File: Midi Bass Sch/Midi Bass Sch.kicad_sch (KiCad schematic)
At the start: 0 parts

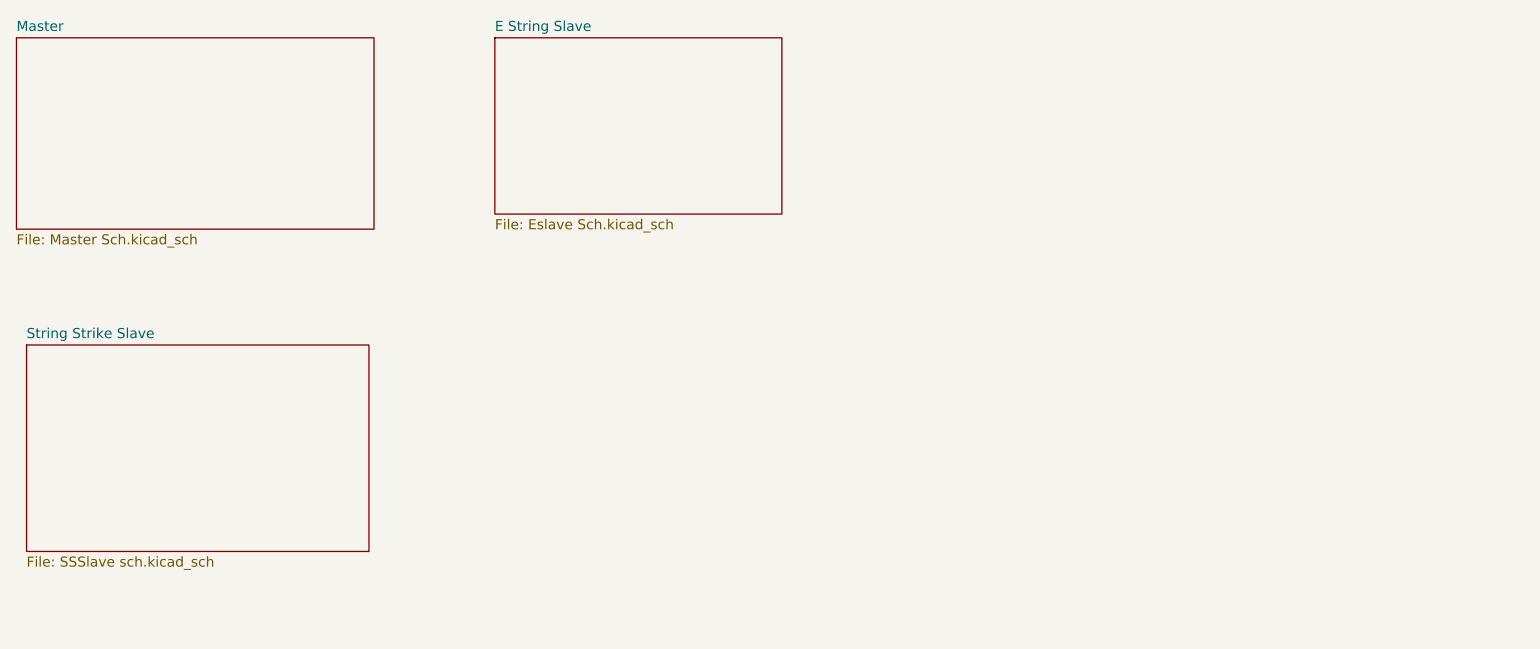
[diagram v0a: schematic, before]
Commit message: updated schematic to include all slaves
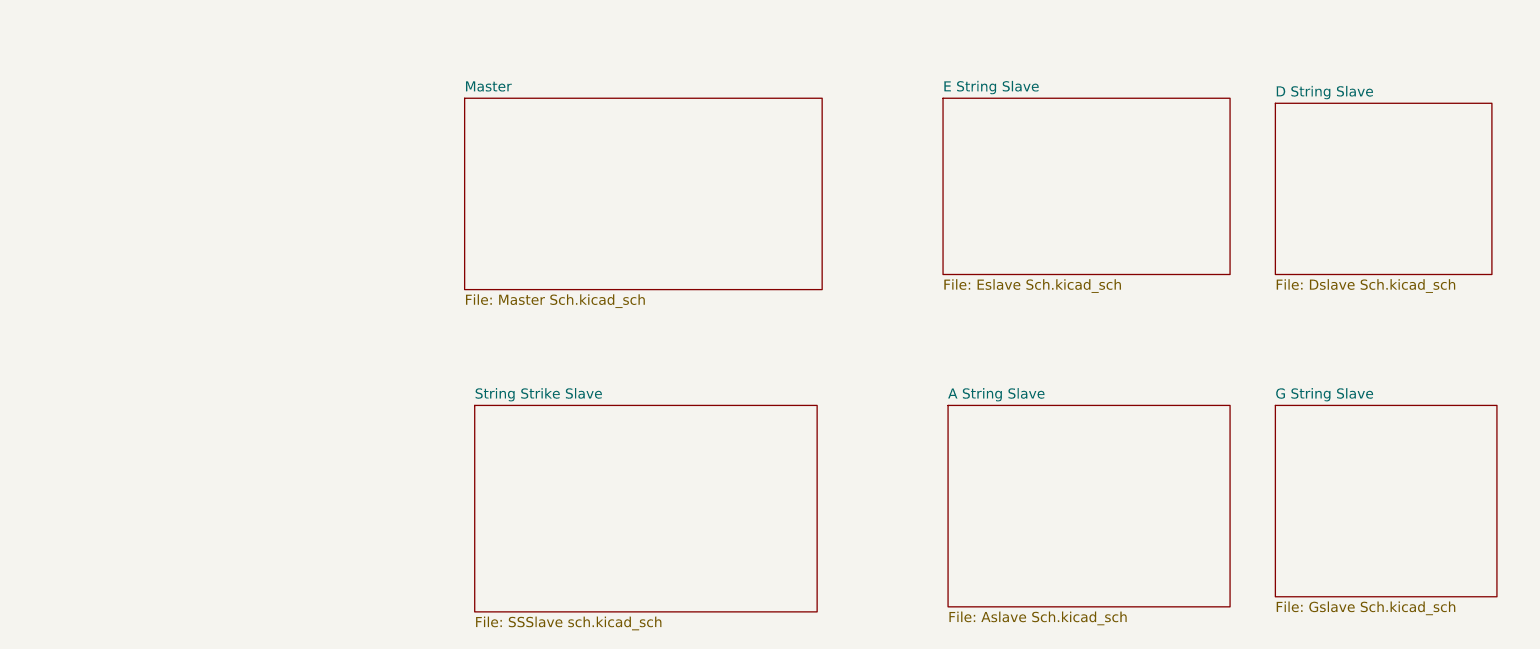
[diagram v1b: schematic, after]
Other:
- added sheet A String Slave (Aslave Sch.kicad_sch)
- added sheet D String Slave (Dslave Sch.kicad_sch)
- added sheet G String Slave (Gslave Sch.kicad_sch)
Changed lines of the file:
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@@
 	(paper "A4")
 	(sheet
-		(at 40.64 43.815)
+		(at 97.155 51.435)
 		(size 45.085 24.13)
 		(fields_autoplaced yes)
@@
 		)
 		(property "Sheetname" "Master"
-			(at 40.64 43.1034 0)
+			(at 97.155 50.7234 0)
 			(effects
 				(font
@@
 		)
 		(property "Sheetfile" "Master Sch.kicad_sch"
-			(at 40.64 68.5296 0)
+			(at 97.155 76.1496 0)
 			(effects
 				(font
@@
 	)
 	(sheet
-		(at 100.965 43.815)
+		(at 199.39 52.07)
+		(size 27.305 21.59)
+		(fields_autoplaced yes)
+		(stroke
+			(width 0.1524)
+			(type solid)
+		)
+		(fill
+			(color 255 255 194 1.0000)
+		)
+		(property "Sheetname" "D String Slave"
+			(at 199.39 51.3584 0)
+			(effects
+				(font
+					(size 1.27 1.27)
+				)
+				(justify left bottom)
+			)
+		)
+		(property "Sheetfile" "Dslave Sch.kicad_sch"
+			(at 199.39 74.2446 0)
+			(effects
+				(font
+					(size 1.27 1.27)
+				)
+				(justify left top)
+			)
+		)
+		(instances
+			(project "Midi Bass Sch"
+				(path "/06818073-fb22-48ee-acc5-6dedd827034e"
+					(page "7")
+				)
+			)
+		)
+	)
+	(sheet
+		(at 157.48 51.435)
 		(size 36.195 22.225)
 		(fields_autoplaced yes)
@@
 		)
 		(property "Sheetname" "E String Slave"
-			(at 100.965 43.1034 0)
+			(at 157.48 50.7234 0)
 			(effects
 				(font
@@
 		)
 		(property "Sheetfile" "Eslave Sch.kicad_sch"
-			(at 100.965 66.6246 0)
+			(at 157.48 74.2446 0)
 			(effects
 				(font
@@
 	)
 	(sheet
-		(at 41.91 82.55)
+		(at 98.425 90.17)
 		(size 43.18 26.035)
 		(fields_autoplaced yes)
@@
 		)
 		(property "Sheetname" "String Strike Slave"
-			(at 41.91 81.8384 0)
+			(at 98.425 89.4584 0)
 			(effects
 				(font
@@
 		)
 		(property "Sheetfile" "SSSlave sch.kicad_sch"
-			(at 41.91 109.1696 0)
+			(at 98.425 116.7896 0)
 			(effects
 				(font
@@
 				)
 			)
+		)
+	)
+	(sheet
+		(at 199.39 90.17)
+		(size 27.94 24.13)
+		(fields_autoplaced yes)
+		(stroke
+			(width 0.1524)
+			(type solid)
+		)
+		(fill
+			(color 255 255 194 1.0000)
+		)
+		(property "Sheetname" "G String Slave"
+			(at 199.39 89.4584 0)
+			(effects
+				(font
+					(size 1.27 1.27)
+				)
+				(justify left bottom)
+			)
+		)
+		(property "Sheetfile" "Gslave Sch.kicad_sch"
+			(at 199.39 114.8846 0)
+			(effects
+				(font
+					(size 1.27 1.27)
+				)
+				(justify left top)
+			)
+		)
+		(instances
+			(project "Midi Bass Sch"
+				(path "/06818073-fb22-48ee-acc5-6dedd827034e"
+					(page "8")
+				)
+			)
+		)
+	)
+	(sheet
+		(at 158.115 90.17)
+		(size 35.56 25.4)
+		(fields_autoplaced yes)
+		(stroke
+			(width 0.1524)
+			(type solid)
+		)
+		(fill
+			(color 255 255 194 1.0000)
+		)
+		(property "Sheetname" "A String Slave"
+			(at 158.115 89.4584 0)
+			(effects
+				(font
+					(size 1.27 1.27)
+				)
+				(justify left bottom)
+			)
+		)
+		(property "Sheetfile" "Aslave Sch.kicad_sch"
+			(at 158.115 116.1546 0)
+			(effects
+				(font
+					(size 1.27 1.27)
+				)
+				(justify left top)
+			)
+		)
+		(instances
+			(project "Midi Bass Sch"
+				(path "/06818073-fb22-48ee-acc5-6dedd827034e"
+					(page "6")
+				)
+			)

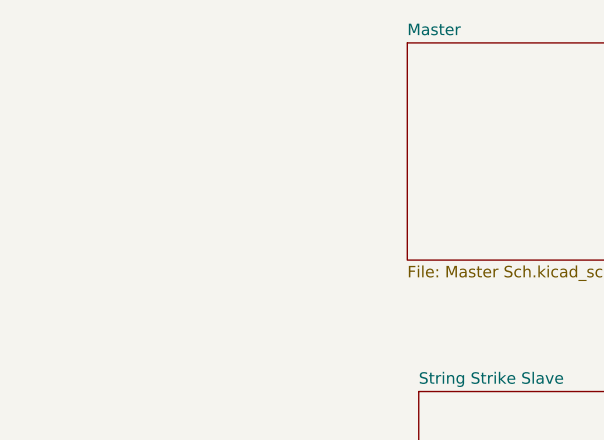
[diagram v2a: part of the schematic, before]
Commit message: added schematic page for power
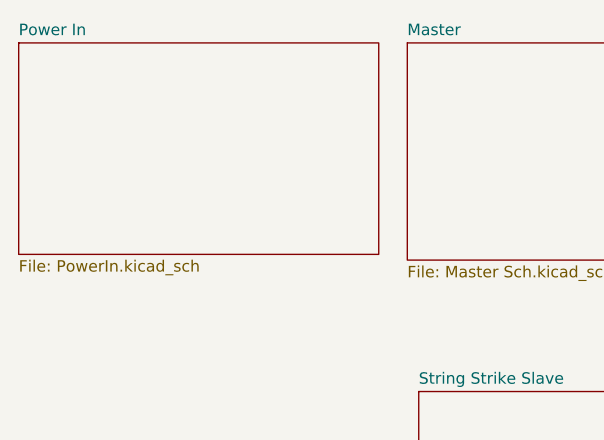
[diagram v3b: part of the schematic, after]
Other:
- added sheet Power In (PowerIn.kicad_sch)
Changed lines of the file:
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@@
+	)
+	(sheet
+		(at 53.975 51.435)
+		(size 40.005 23.495)
+		(fields_autoplaced yes)
+		(stroke
+			(width 0.1524)
+			(type solid)
+		)
+		(fill
+			(color 255 255 194 1.0000)
+		)
+		(property "Sheetname" "Power In"
+			(at 53.975 50.7234 0)
+			(effects
+				(font
+					(size 1.27 1.27)
+				)
+				(justify left bottom)
+			)
+		)
+		(property "Sheetfile" "PowerIn.kicad_sch"
+			(at 53.975 75.5146 0)
+			(effects
+				(font
+					(size 1.27 1.27)
+				)
+				(justify left top)
+			)
+		)
+		(instances
+			(project "Midi Bass Sch"
+				(path "/06818073-fb22-48ee-acc5-6dedd827034e"
+					(page "13")
+				)
+			)
+		)
 	)
 	(sheet

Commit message: began getting images for schematic appendix
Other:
- title: (none) -> MIDI Bass Guitar Schmatic
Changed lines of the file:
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@@
 	(generator_version "8.0")
 	(paper "A")
+	(title_block
+		(title "MIDI Bass Guitar Schmatic")
+		(date "2024-12-10")
+		(rev "A")
+	)
 	(sheet
 		(at 97.155 51.435)

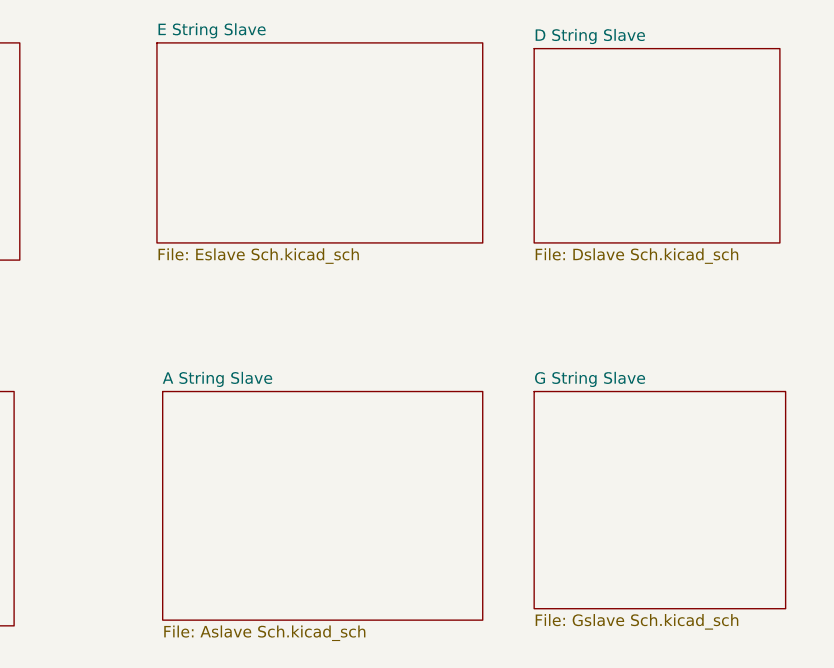
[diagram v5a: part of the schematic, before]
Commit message: removed sheets of master schematic to match new design
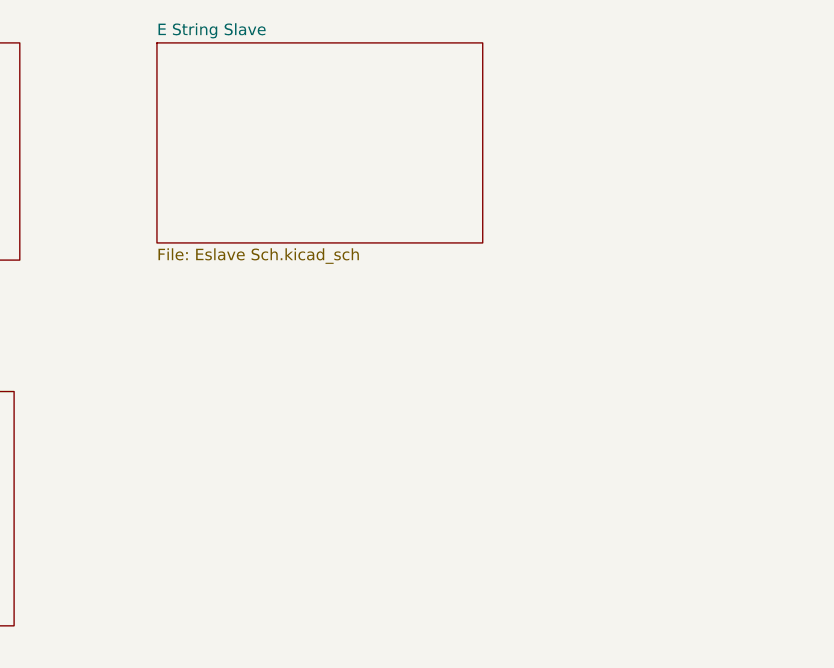
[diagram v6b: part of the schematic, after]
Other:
- removed sheet A String Slave
- removed sheet D String Slave
- removed sheet G String Slave
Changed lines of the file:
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@@
-	)
-	(sheet
-		(at 199.39 52.07)
-		(size 27.305 21.59)
-		(exclude_from_sim no)
-		(in_bom yes)
-		(on_board yes)
-		(dnp no)
-		(fields_autoplaced yes)
-		(stroke
-			(width 0.1524)
-			(type solid)
-		)
-		(fill
-			(color 255 255 194 1.0000)
-		)
-		(property "Sheetname" "D String Slave"
-			(at 199.39 51.3584 0)
-			(effects
-				(font
-					(size 1.27 1.27)
-				)
-				(justify left bottom)
-			)
-		)
-		(property "Sheetfile" "Dslave Sch.kicad_sch"
-			(at 199.39 74.2446 0)
-			(effects
-				(font
-					(size 1.27 1.27)
-				)
-				(justify left top)
-			)
-		)
-		(instances
-			(project "Midi Bass Sch"
-				(path "/06818073-fb22-48ee-acc5-6dedd827034e"
-					(page "7")
-				)
-			)
-		)
 	)
 	(sheet
@@
 	)
 	(sheet
-		(at 199.39 90.17)
-		(size 27.94 24.13)
-		(exclude_from_sim no)
-		(in_bom yes)
-		(on_board yes)
-		(dnp no)
-		(fields_autoplaced yes)
-		(stroke
-			(width 0.1524)
-			(type solid)
-		)
-		(fill
-			(color 255 255 194 1.0000)
-		)
-		(property "Sheetname" "G String Slave"
-			(at 199.39 89.4584 0)
-			(effects
-				(font
-					(size 1.27 1.27)
-				)
-				(justify left bottom)
-			)
-		)
-		(property "Sheetfile" "Gslave Sch.kicad_sch"
-			(at 199.39 114.8846 0)
-			(effects
-				(font
-					(size 1.27 1.27)
-				)
-				(justify left top)
-			)
-		)
-		(instances
-			(project "Midi Bass Sch"
-				(path "/06818073-fb22-48ee-acc5-6dedd827034e"
-					(page "8")
-				)
-			)
-		)
-	)
-	(sheet
 		(at 53.975 51.435)
 		(size 40.005 23.495)
@@
 				)
 			)
-		)
-	)
-	(sheet
-		(at 158.115 90.17)
-		(size 35.56 25.4)
-		(exclude_from_sim no)
-		(in_bom yes)
-		(on_board yes)
-		(dnp no)
-		(fields_autoplaced yes)
-		(stroke
-			(width 0.1524)
-			(type solid)
-		)
-		(fill
-			(color 255 255 194 1.0000)
-		)
-		(property "Sheetname" "A String Slave"
-			(at 158.115 89.4584 0)
-			(effects
-				(font
-					(size 1.27 1.27)
-				)
-				(justify left bottom)
-			)
-		)
-		(property "Sheetfile" "Aslave Sch.kicad_sch"
-			(at 158.115 116.1546 0)
-			(effects
-				(font
-					(size 1.27 1.27)
-				)
-				(justify left top)
-			)
-		)
-		(instances
-			(project "Midi Bass Sch"
-				(path "/06818073-fb22-48ee-acc5-6dedd827034e"
-					(page "6")
-				)
-			)
